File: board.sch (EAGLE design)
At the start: 85 parts, among them J1 AVR_SPI_PRG_6NS, U2 USD-SOCKETNEW, U3 MAX1555, U4 TPS2112A, U6 74HC595, U7 3.3V, U8 2.8V, Y1 12.288MHz, Y2 8MHz

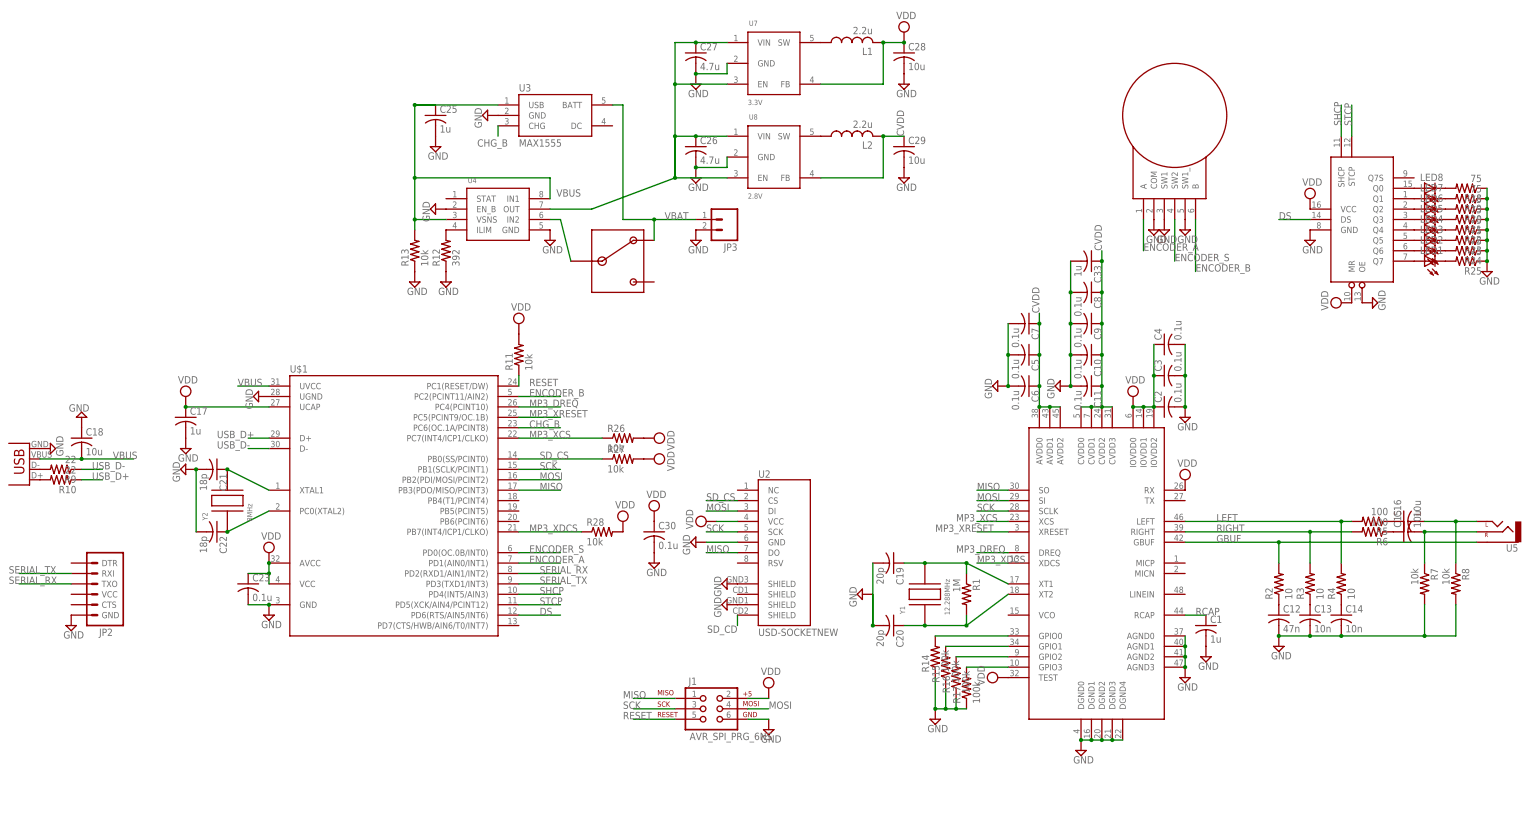
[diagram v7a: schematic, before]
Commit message: Renumbered parts
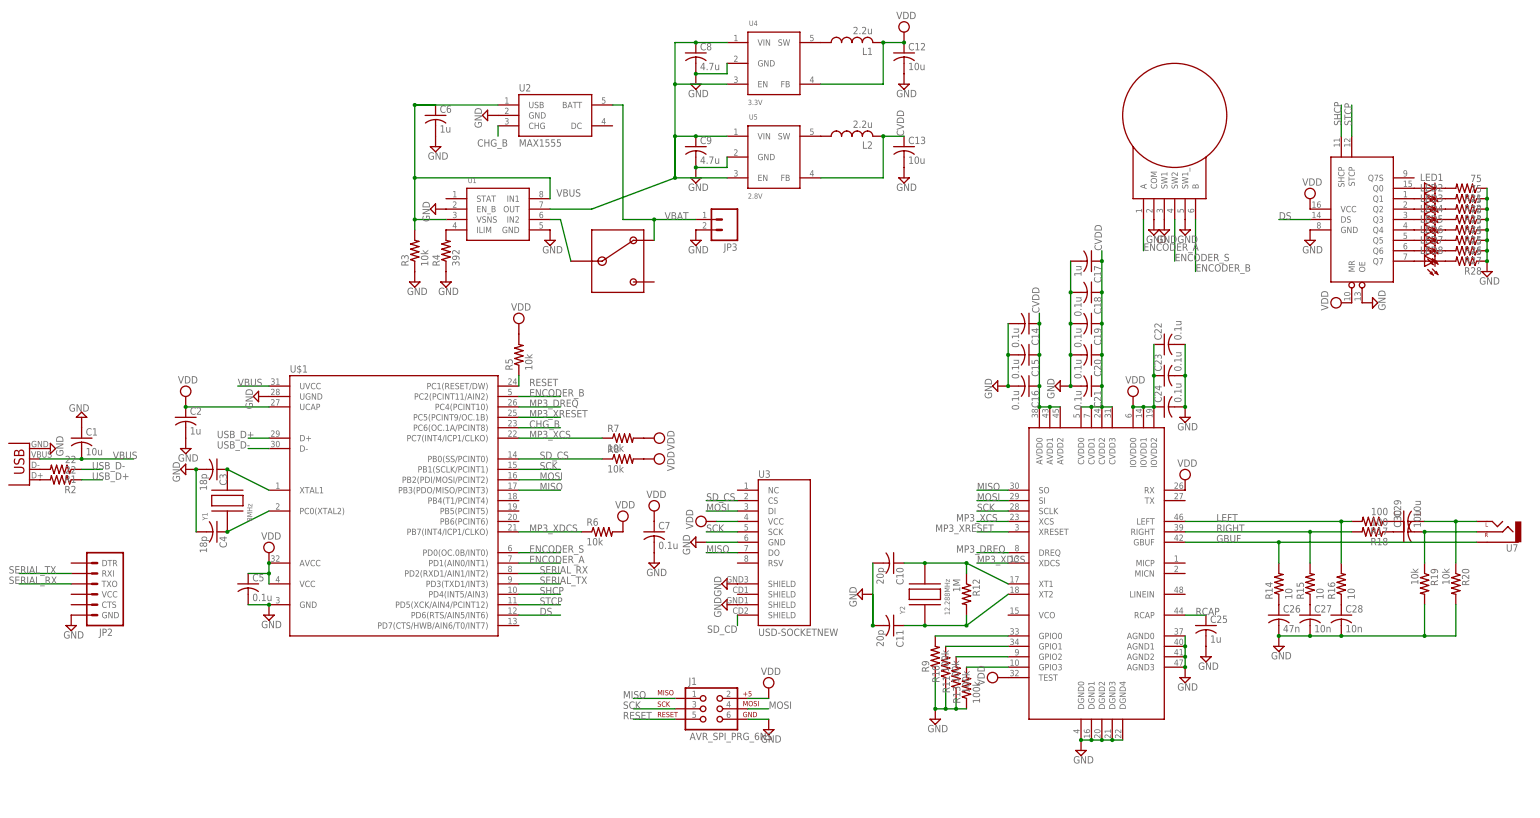
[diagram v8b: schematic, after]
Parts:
- removed C33: 1u, rcl:C-USC0603K
- removed S4: JS102011SAQN, mkmp3:JS102011SAQN
- removed U8: 2.8V, mkmp3:LM3671
- added C24: 0.1u, rcl:C-USC0603K
- added S2: EVQ-WKA, mkmp3:EVQ-WKA
- added U1: TPS2112A, mkmp3:TPS2112A
- C1: value 1u -> 10u
- C10, C11: value 0.1u -> 20p
- C12: value 47n -> 10u
- C13: value 10n -> 10u
- C14: value 10n -> 0.1u
- C15, C16, C18: value 10u -> 0.1u
- C19, C20: value 20p -> 0.1u
- C2, C6: value 0.1u -> 1u
- C21, C22: value 18p -> 0.1u
- C26: value 4.7u -> 47n
- C27: value 4.7u -> 10n
- C28: value 10u -> 10n
- C3, C4: value 0.1u -> 18p
- C30: value 0.1u -> 10u
- C8, C9: value 0.1u -> 4.7u
- R1: value 1M -> 22
- R10: value 22 -> 100k
- R11, R13: value 10k -> 100k; device rcl:R-US_R0603 -> rcl:R-US_R0603W
- R12: value 392 -> 1M
- R14, R16: value 100k -> 10
- R15: value 100k -> 10; device rcl:R-US_R0603 -> rcl:R-US_R0603W
- R17: value 100k -> 100
- R18: value 75 -> 100
- R19, R20: value 75 -> 10k
- R2: value 10 -> 22; device rcl:R-US_R0603W -> rcl:R-US_R0603
- R26, R28: value 10k -> 75
- R27: value 10k -> 75; device rcl:R-US_R0603 -> rcl:R-US_R0603W
- R3: value 10 -> 10k; device rcl:R-US_R0603W -> rcl:R-US_R0603
- R4: value 10 -> 392; device rcl:R-US_R0603W -> rcl:R-US_R0603
- R5: value 100 -> 10k; device rcl:R-US_R0603W -> rcl:R-US_R0603
- R6: value 100 -> 10k
- R8: device rcl:R-US_R0603W -> rcl:R-US_R0603
- R9: value 22 -> 100k; device rcl:R-US_R0603 -> rcl:R-US_R0603W
- S1: value EVQ-WKA -> JS102011SAQN; device mkmp3:EVQ-WKA -> mkmp3:JS102011SAQN
- U2: value USD-SOCKETNEW -> MAX1555; device SparkFun-Connectors:USD-SOCKETNEW -> SparkFun-PowerIC:MAX1555
- U3: value MAX1555 -> USD-SOCKETNEW; device SparkFun-PowerIC:MAX1555 -> SparkFun-Connectors:USD-SOCKETNEW
- U4: value TPS2112A -> 3.3V; device mkmp3:TPS2112A -> mkmp3:LM3671
- U5: value (none) -> 2.8V; device SparkFun-Connectors:AUDIO-JACKSMD2 -> mkmp3:LM3671
- U7: value 3.3V -> (none); device mkmp3:LM3671 -> SparkFun-Connectors:AUDIO-JACKSMD2
- Y1: value 12.288MHz -> 8MHz; device mkmp3:CSM-3X -> mkmp3:CSM-7X
- Y2: value 8MHz -> 12.288MHz; device mkmp3:CSM-7X -> mkmp3:CSM-3X
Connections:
- removed net N$29 (its old number): LED6.C, R20.2
- new net N$32: LED6.C, R26.2
- net CHG_B: now also U2.CHG; no longer U3.CHG
- net CVDD: now also C13.1, C14.1, C15.1, C16.1, C17.1, C18.1, C19.1, C20.1, C21.1, U5.FB; no longer C10.1, C11.1, C29.1, C33.1, C5.1, C6.1, C7.1, C8.1, C9.1, U8.FB
- net ENCODER_A: now also S2.A; no longer S1.A
- net ENCODER_B: now also S2.B; no longer S1.B
- net ENCODER_S: now also S2.SW2; no longer S1.SW2
- net GBUF: now also R14.2, U7.SLEEVE; no longer R2.2, U5.SLEEVE
- net GND: now also C1.1, C15.2, C16.2, C18.2, C24.2, R10.1, R11.1, R19.2, R20.2, R26.1, R27.1, R28.1, R3.1, R4.1, R9.1, S2.COM, S2.SW1, S2.SW1_, U1.EN_B, U1.GND, U3.SHIELD@1, U3.SHIELD@3, U5.GND; no longer C1.2, C18.1, C29.2, C30.2, C33.2, R12.1, R14.1, R15.1, R16.1, R17.1, R18.1, R19.1, R20.1, R7.2, R8.2, S1.COM, S1.SW1, S1.SW1_, U2.SHIELD@1, U2.SHIELD@3, U4.EN_B, U7.GND, U8.GND
- net GPIO0: now also R9.2; no longer R14.2
- net GPIO1: now also R10.2; no longer R15.2
- net GPIO2: now also R11.2; no longer R16.2
- net GPIO3: now also R13.2; no longer R17.2
- net LEFT: now also R16.2, R17.2; no longer R4.2, R5.2
- net MISO: now also U3.DO; no longer U2.DO
- net MOSI: now also U3.DI; no longer U2.DI
- net MP3_XCS: now also R7.1; no longer R26.1
- net MP3_XDCS: now also R6.1; no longer R28.1
- net N$1: now also R1.2; no longer R9.2
- net N$10: now also C30.1, R18.1; no longer C15.1, R6.1
- net N$11: now also C29.1, R17.1; no longer C16.1, R5.1
- net N$12: now also C30.2, R19.1, U7.RIGHT; no longer C15.2, R7.1, U5.RIGHT
- net N$13: now also C29.2, R20.1, U7.LEFT; no longer C16.2, R8.1, U5.LEFT
- net N$14: now also C4.1, Y1.P$1; no longer C22.1, Y2.P$1
- net N$17: now also R4.2, U1.ILIM; no longer R12.2, U4.ILIM
- net N$18: now also C8.1, C9.1, U1.OUT, U4.EN, U4.VIN, U5.EN, U5.VIN; no longer C26.1, C27.1, U4.OUT, U7.EN, U7.VIN, U8.EN, U8.VIN
- net N$19: now also LED8.A; no longer LED1.A
- net N$2: now also C3.1, Y1.P$2; no longer C21.1, Y2.P$2
- net N$20: now also LED7.A; no longer LED2.A
- net N$21: now also LED6.A; no longer LED3.A
- net N$22: now also LED5.A; no longer LED4.A
- net N$23: now also LED4.A; no longer LED5.A
- net N$24: now also LED3.A; no longer LED6.A
- net N$25: now also LED2.A; no longer LED7.A
- net N$26: now also LED1.A; no longer LED8.A
- net N$27: now also LED1.C, R21.2; no longer LED8.C, R18.2
- net N$28: now also LED2.C, R22.2; no longer LED7.C, R19.2
- net N$3: now also C26.1, R14.1; no longer C12.1, R2.1
- net N$30: now also LED4.C, R24.2; no longer LED5.C, R21.2
- net N$31: now also LED5.C, R25.2; no longer LED4.C, R22.2
- net N$33: now also LED7.C, R27.2; no longer LED2.C, R24.2
- net N$34: now also LED8.C, R28.2; no longer LED1.C, R25.2
- net N$35: now also U4.SW; no longer U7.SW
- net N$36: now also U5.SW; no longer U8.SW
- net N$37: now also S1.2, U1.IN2; no longer S4.2, U4.IN2
- net N$4: now also C27.1, R15.1; no longer C13.1, R3.1
- net N$5: now also C28.1, R16.1; no longer C14.1, R4.1
- net N$6: now also R2.2; no longer R10.2
- net N$7: now also C11.1, R12.2, Y2.P$1; no longer C20.1, R1.2, Y1.P$1
- net N$8: now also C10.1, R12.1, Y2.P$2; no longer C19.1, R1.1, Y1.P$2
- net RCAP: now also C25.1; no longer C1.1
- net RESET: now also R5.1; no longer R11.1
- net RIGHT: now also R15.2, R18.2; no longer R3.2, R6.2
- net SCK: now also U3.SCK; no longer U2.SCK
- net SD_CD: now also U3.SHIELD@4; no longer U2.SHIELD@4
- net SD_CS: now also R8.1, U3.CS; no longer R27.1, U2.CS
- net USB_D+: now also R2.1; no longer R10.1
- net USB_D-: now also R1.1; no longer R9.1
- net VBAT: now also S1.3, U2.BATT; no longer S4.3, U3.BATT
- net VBUS: now also C1.2, C6.1, R3.2, U1.IN1, U1.VSNS, U2.USB; no longer C18.2, C25.1, R13.2, U3.USB, U4.IN1, U4.VSNS
- net VDD: now also C12.1, C22.1, C24.1, C5.1, C7.1, R5.2, R6.2, R7.2, R8.2, U3.VCC, U4.FB; no longer C17.1, C28.1, C3.1, C30.1, C4.1, R11.2, R26.2, R27.2, R28.2, U2.VCC, U7.FB
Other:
- moved on the sheet: C1, C10, C11, C12, C13, C14, C15, C16, C17, C18, C19, C2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
